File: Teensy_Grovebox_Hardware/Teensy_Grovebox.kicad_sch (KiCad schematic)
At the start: 136 parts, among them J1 USB4085-GF-A_REVA4, J10 AudioJack4_HP, J2 Batt connector, J3 Batt connector, J4 Conn_SUSTAIN, J5 Conn_I2C, J6 Conn_SPDIF, J7 Conn_01x02, J8 AudioJack4_LineIN, J9 AudioJack4_LineOUT, Q1 IRF4905, Q2 IRF4905, Q3 2N7000, SW1 SW_WKEY, SW10 SW_WKEY, SW11 SW_BKEY, SW12 SW_WKEY, SW13 SW_WKEY, SW14 SW_BKEY, SW15 SW_WKEY, SW16 SW_BKEY, SW17 SW_WKEY, SW18 SW_WKEY, SW19 SW_BKEY, SW2 SW_BKEY, SW20 SW_WKEY, SW21 SW_BKEY, SW22 SW_WKEY, SW23 SW_BKEY, SW24 SW_WKEY, SW25 SW_WKEY, SW26 SW_Push, SW27 SW_Push, SW28 SW_Push, SW29 SW_Push, SW3 SW_WKEY, SW30 SW_Push, SW31 SW_Push, SW32 SW_Push, SW33 SW_Push, SW34 SW_Push, SW4 SW_BKEY, SW5 SW_WKEY, SW6 SW_WKEY, SW7 SW_BKEY, SW8 SW_WKEY, SW9 SW_BKEY, U1 ILI9431_32_TFT, U10 Pololu_5v_booster, U11 AMS1117-3.3, U12 LP5907MFX-3.3, U2 Teensy4.0_AudioShield_REVD, U3 Teensy4.1, U4 MCP23017_SO, U5 MCP23017_SO, U6 PAM8403D, U7 LM3914V, U8 LM3914V, U9 TP4056

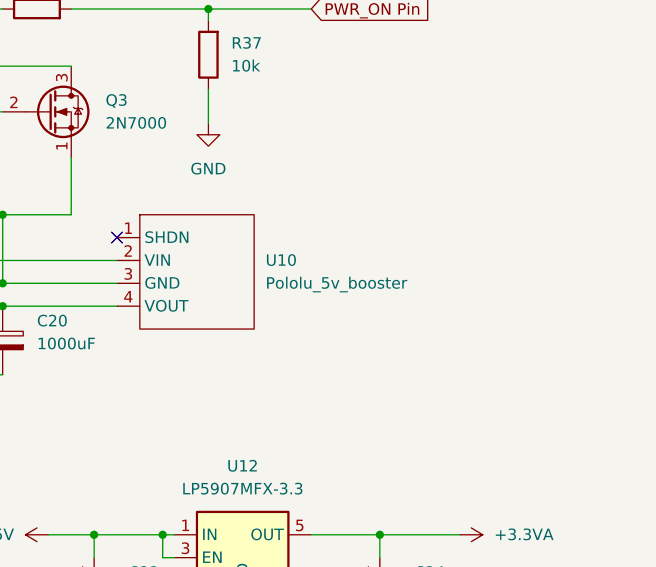
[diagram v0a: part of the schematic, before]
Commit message: Include 5v booster model number in PCB files.
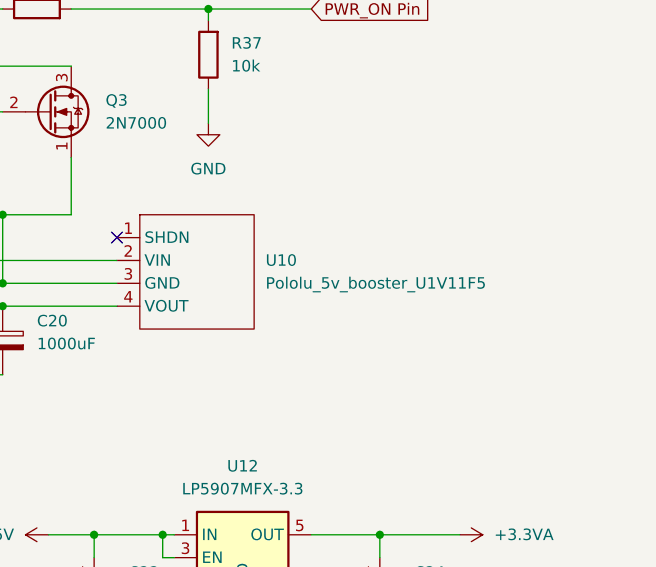
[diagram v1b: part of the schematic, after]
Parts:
- U10: value Pololu_5v_booster -> Pololu_5v_booster_U1V11F5
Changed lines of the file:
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@@
       (effects (font (size 1.27 1.27)) (justify left))
     )
-    (property "Value" "Pololu_5v_booster" (id 1) (at 532.13 215.8999 0)
+    (property "Value" "Pololu_5v_booster_U1V11F5" (id 1) (at 532.13 215.8999 0)
       (effects (font (size 1.27 1.27)) (justify left))
     )
@@
     )
     (path "/286a35d1-1b8e-46db-8579-f61f4c470a7a"
-      (reference "U10") (unit 1) (value "Pololu_5v_booster") (footprint "OTHER:POLOLU_5V_BOOST")
+      (reference "U10") (unit 1) (value "Pololu_5v_booster_U1V11F5") (footprint "OTHER:POLOLU_5V_BOOST")
     )
     (path "/96c75bfb-082e-4283-b7dd-656219c78d93"
